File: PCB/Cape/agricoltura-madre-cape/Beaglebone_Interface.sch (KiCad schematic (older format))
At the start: 2 parts, among them P8 BeagleBone_Black_Header, P9 BeagleBone_Black_Header

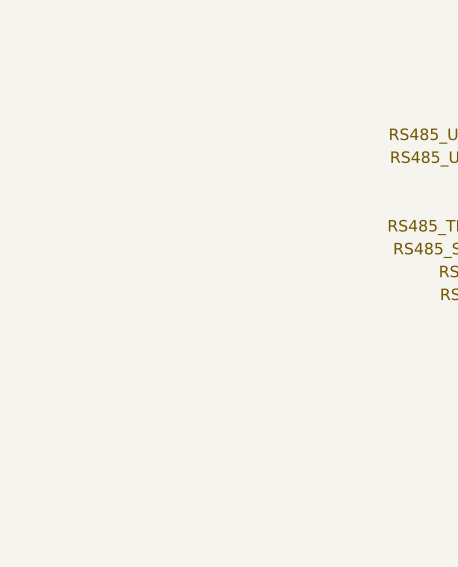
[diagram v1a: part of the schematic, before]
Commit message: SPI UART Bridge
Fleshed out schematic for SPI UART bridge chip, realized we may not need it, now going to fork project and develop two versions in this same repository.
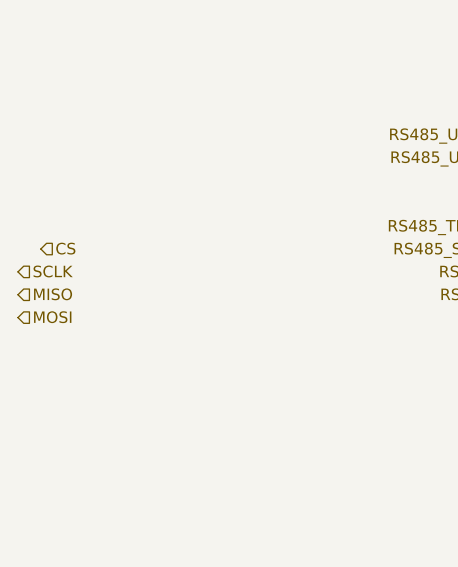
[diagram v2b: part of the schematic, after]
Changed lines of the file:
@@
 Wire Wire Line
 	3450 3550 4350 3550
+Text HLabel 1150 3650 2    50   Input ~ 0
+SCLK
+Text HLabel 1150 3750 2    50   Input ~ 0
+MISO
+Text HLabel 1150 3850 2    50   Input ~ 0
+MOSI
+Text HLabel 1250 3550 2    50   Input ~ 0
+CS
 $EndSCHEMATC

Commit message: Datasheets and BBG version
Finished initial schematic for BBG Gateway version and added datasheets for ST sub 1GHZ RF hardware.
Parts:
- added R1, R2, R3, R4, R5: RC0402FR-0733RL, AVR-KiCAD-Lib-Resistors:R0402, symbol AVR-KiCAD-Lib-Resistors:RC0402FR-0733RL
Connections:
- net CS: now also R1.1
- net MISO: now also R2.1
- net MOSI: now also R4.2
- net RS485_SL_RATE1: now also P9.20 (Pin_20); no longer P9.18 (Pin_18)
- net RS485_SL_RATE2: now also P9.27 (Pin_27); no longer P9.21 (Pin_21)
- net RS485_TERM_EN2: now also P9.29 (Pin_29); no longer P9.19 (Pin_19)
- net SCLK: now also R5.2
- net SPI0_CS0: now reaches P9.17 (Pin_17)
- net SPI0_CS0: now also R1.2
- net SPI0_SCLK: now reaches P9.22 (Pin_22)
- net SPI0_SCLK: now also R5.1
- net GNDD renamed GND
- new net: P9.19 (Pin_19), R3.2
- new net SHDN: R3.1
- new net SPI0_D0: P9.21 (Pin_21), R2.2
- new net SPI0_D1: P9.18 (Pin_18), R4.1
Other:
- moved on the sheet: P8

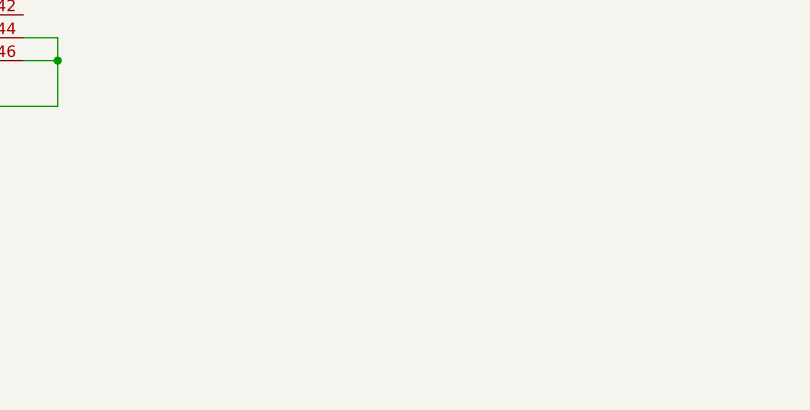
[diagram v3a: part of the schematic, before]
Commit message: Board Work
Board shape added working on cut outs
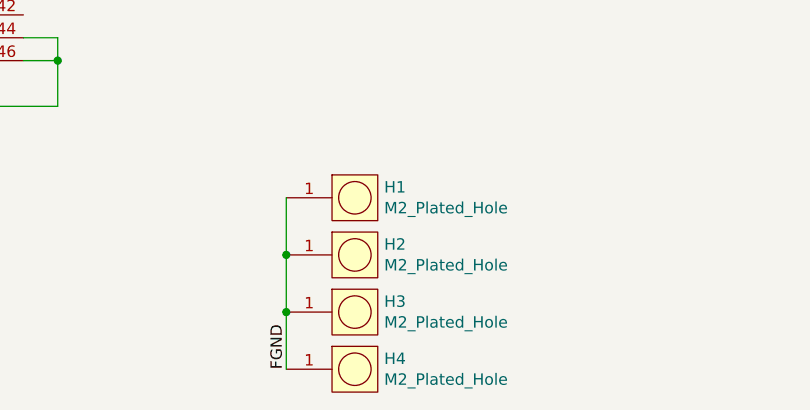
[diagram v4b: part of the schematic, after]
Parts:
- added H1, H2, H3, H4: M2_Plated_Hole, AVR-KiCAD-Lib-Holes_Fasteners:M2_HOLE, symbol AVR-KiCAD-Lib-Holes_Fasteners:M2_Plated_Hole
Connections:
- new net FGND: H1.1, H2.1, H3.1, H4.1
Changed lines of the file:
@@
 Text Label 5250 3350 0    50   ~ 0
 SPI0_D1
+$Comp
+L AVR-KiCAD-Lib-Holes_Fasteners:M2_Plated_Hole H1
+U 1 1 5F30F66E
+P 6200 5350
+F 0 "H1" H 6428 5396 50  0000 L CNN
+F 1 "M2_Plated_Hole" H 6428 5305 50  0000 L CNN
+F 2 "AVR-KiCAD-Lib-Holes_Fasteners:M2_HOLE" H 6200 5350 50  0001 C CNN
+F 3 "" H 6200 5350 50  0001 C CNN
+F 4 "*" H 6300 5600 50  0001 C CNN "Cost QTY: 1"
+F 5 "*" H 6400 5700 50  0001 C CNN "Cost QTY: 1000"
+F 6 "*" H 6500 5800 50  0001 C CNN "Cost QTY: 2500"
+F 7 "*" H 6600 5900 50  0001 C CNN "Cost QTY: 5000"
+F 8 "*" H 6700 6000 50  0001 C CNN "Cost QTY: 10000"
+F 9 "*" H 6800 6100 50  0001 C CNN "MFR"
+F 10 "*" H 6900 6200 50  0001 C CNN "MFR#"
+F 11 "*" H 7000 6300 50  0001 C CNN "Vendor"
+F 12 "*" H 7100 6400 50  0001 C CNN "Vendor #"
+F 13 "*" H 7200 6500 50  0001 C CNN "Designer"
+F 14 "*" H 7300 6600 50  0001 C CNN "Height"
+F 15 "*" H 8400 7700 50  0001 C CNN "Date Created"
+F 16 "*" H 7400 6700 50  0001 C CNN "Date Modified"
+F 17 "*" H 7500 6800 50  0001 C CNN "Lead-Free ?"
+F 18 "*" H 7600 6900 50  0001 C CNN "RoHS Levels"
+F 19 "*" H 7700 7000 50  0001 C CNN "Mounting"
+F 20 "*" H 7800 7100 50  0001 C CNN "Pin Count #"
+F 21 "*" H 7900 7200 50  0001 C CNN "Status"
+F 22 "*" H 8000 7300 50  0001 C CNN "Tolerance"
+F 23 "*" H 8100 7400 50  0001 C CNN "Type"
+F 24 "*" H 8200 7500 50  0001 C CNN "Voltage"
+F 25 "*" H 8300 7650 50  0001 C CNN "Package"
+F 26 "M2 Hole" H 8500 7850 50  0001 C CNN "_Value_"
+F 27 "*" H 8600 7950 50  0001 C CNN "Management_ID"
+F 28 "Plated M2 Screw Hole" H 8600 7950 50  0001 C CNN "Description"
+	1    6200 5350
+	1    0    0    -1
+$EndComp
+$Comp
+L AVR-KiCAD-Lib-Holes_Fasteners:M2_Plated_Hole H2
+U 1 1 5F3101E5
+P 6200 5600
+F 0 "H2" H 6428 5646 50  0000 L CNN
+F 1 "M2_Plated_Hole" H 6428 5555 50  0000 L CNN
+F 2 "AVR-KiCAD-Lib-Holes_Fasteners:M2_HOLE" H 6200 5600 50  0001 C CNN
+F 3 "" H 6200 5600 50  0001 C CNN
+F 4 "*" H 6300 5850 50  0001 C CNN "Cost QTY: 1"
+F 5 "*" H 6400 5950 50  0001 C CNN "Cost QTY: 1000"
+F 6 "*" H 6500 6050 50  0001 C CNN "Cost QTY: 2500"
+F 7 "*" H 6600 6150 50  0001 C CNN "Cost QTY: 5000"
+F 8 "*" H 6700 6250 50  0001 C CNN "Cost QTY: 10000"
+F 9 "*" H 6800 6350 50  0001 C CNN "MFR"
+F 10 "*" H 6900 6450 50  0001 C CNN "MFR#"
+F 11 "*" H 7000 6550 50  0001 C CNN "Vendor"
+F 12 "*" H 7100 6650 50  0001 C CNN "Vendor #"
+F 13 "*" H 7200 6750 50  0001 C CNN "Designer"
+F 14 "*" H 7300 6850 50  0001 C CNN "Height"
+F 15 "*" H 8400 7950 50  0001 C CNN "Date Created"
+F 16 "*" H 7400 6950 50  0001 C CNN "Date Modified"
+F 17 "*" H 7500 7050 50  0001 C CNN "Lead-Free ?"
+F 18 "*" H 7600 7150 50  0001 C CNN "RoHS Levels"
+F 19 "*" H 7700 7250 50  0001 C CNN "Mounting"
+F 20 "*" H 7800 7350 50  0001 C CNN "Pin Count #"
+F 21 "*" H 7900 7450 50  0001 C CNN "Status"
+F 22 "*" H 8000 7550 50  0001 C CNN "Tolerance"
+F 23 "*" H 8100 7650 50  0001 C CNN "Type"
+F 24 "*" H 8200 7750 50  0001 C CNN "Voltage"
+F 25 "*" H 8300 7900 50  0001 C CNN "Package"
+F 26 "M2 Hole" H 8500 8100 50  0001 C CNN "_Value_"
+F 27 "*" H 8600 8200 50  0001 C CNN "Management_ID"
+F 28 "Plated M2 Screw Hole" H 8600 8200 50  0001 C CNN "Description"
+	1    6200 5600
+	1    0    0    -1
+$EndComp
+$Comp
+L AVR-KiCAD-Lib-Holes_Fasteners:M2_Plated_Hole H3
+U 1 1 5F310E62
+P 6200 5850
+F 0 "H3" H 6428 5896 50  0000 L CNN
+F 1 "M2_Plated_Hole" H 6428 5805 50  0000 L CNN
+F 2 "AVR-KiCAD-Lib-Holes_Fasteners:M2_HOLE" H 6200 5850 50  0001 C CNN
+F 3 "" H 6200 5850 50  0001 C CNN
+F 4 "*" H 6300 6100 50  0001 C CNN "Cost QTY: 1"
+F 5 "*" H 6400 6200 50  0001 C CNN "Cost QTY: 1000"
+F 6 "*" H 6500 6300 50  0001 C CNN "Cost QTY: 2500"
+F 7 "*" H 6600 6400 50  0001 C CNN "Cost QTY: 5000"
+F 8 "*" H 6700 6500 50  0001 C CNN "Cost QTY: 10000"
+F 9 "*" H 6800 6600 50  0001 C CNN "MFR"
+F 10 "*" H 6900 6700 50  0001 C CNN "MFR#"
+F 11 "*" H 7000 6800 50  0001 C CNN "Vendor"
+F 12 "*" H 7100 6900 50  0001 C CNN "Vendor #"
+F 13 "*" H 7200 7000 50  0001 C CNN "Designer"
+F 14 "*" H 7300 7100 50  0001 C CNN "Height"
+F 15 "*" H 8400 8200 50  0001 C CNN "Date Created"
+F 16 "*" H 7400 7200 50  0001 C CNN "Date Modified"
+F 17 "*" H 7500 7300 50  0001 C CNN "Lead-Free ?"
+F 18 "*" H 7600 7400 50  0001 C CNN "RoHS Levels"
+F 19 "*" H 7700 7500 50  0001 C CNN "Mounting"
+F 20 "*" H 7800 7600 50  0001 C CNN "Pin Count #"
+F 21 "*" H 7900 7700 50  0001 C CNN "Status"
+F 22 "*" H 8000 7800 50  0001 C CNN "Tolerance"
+F 23 "*" H 8100 7900 50  0001 C CNN "Type"
+F 24 "*" H 8200 8000 50  0001 C CNN "Voltage"
+F 25 "*" H 8300 8150 50  0001 C CNN "Package"
+F 26 "M2 Hole" H 8500 8350 50  0001 C CNN "_Value_"
+F 27 "*" H 8600 8450 50  0001 C CNN "Management_ID"
+F 28 "Plated M2 Screw Hole" H 8600 8450 50  0001 C CNN "Description"
+	1    6200 5850
+	1    0    0    -1
+$EndComp
+$Comp
+L AVR-KiCAD-Lib-Holes_Fasteners:M2_Plated_Hole H4
+U 1 1 5F311B49
+P 6200 6100
+F 0 "H4" H 6428 6146 50  0000 L CNN
+F 1 "M2_Plated_Hole" H 6428 6055 50  0000 L CNN
+F 2 "AVR-KiCAD-Lib-Holes_Fasteners:M2_HOLE" H 6200 6100 50  0001 C CNN
+F 3 "" H 6200 6100 50  0001 C CNN
+F 4 "*" H 6300 6350 50  0001 C CNN "Cost QTY: 1"
+F 5 "*" H 6400 6450 50  0001 C CNN "Cost QTY: 1000"
+F 6 "*" H 6500 6550 50  0001 C CNN "Cost QTY: 2500"
+F 7 "*" H 6600 6650 50  0001 C CNN "Cost QTY: 5000"
+F 8 "*" H 6700 6750 50  0001 C CNN "Cost QTY: 10000"
+F 9 "*" H 6800 6850 50  0001 C CNN "MFR"
+F 10 "*" H 6900 6950 50  0001 C CNN "MFR#"
+F 11 "*" H 7000 7050 50  0001 C CNN "Vendor"
+F 12 "*" H 7100 7150 50  0001 C CNN "Vendor #"
+F 13 "*" H 7200 7250 50  0001 C CNN "Designer"
+F 14 "*" H 7300 7350 50  0001 C CNN "Height"
+F 15 "*" H 8400 8450 50  0001 C CNN "Date Created"
+F 16 "*" H 7400 7450 50  0001 C CNN "Date Modified"
+F 17 "*" H 7500 7550 50  0001 C CNN "Lead-Free ?"
+F 18 "*" H 7600 7650 50  0001 C CNN "RoHS Levels"
+F 19 "*" H 7700 7750 50  0001 C CNN "Mounting"
+F 20 "*" H 7800 7850 50  0001 C CNN "Pin Count #"
+F 21 "*" H 7900 7950 50  0001 C CNN "Status"
+F 22 "*" H 8000 8050 50  0001 C CNN "Tolerance"
+F 23 "*" H 8100 8150 50  0001 C CNN "Type"
+F 24 "*" H 8200 8250 50  0001 C CNN "Voltage"
+F 25 "*" H 8300 8400 50  0001 C CNN "Package"
+F 26 "M2 Hole" H 8500 8600 50  0001 C CNN "_Value_"
+F 27 "*" H 8600 8700 50  0001 C CNN "Management_ID"
+F 28 "Plated M2 Screw Hole" H 8600 8700 50  0001 C CNN "Description"
+	1    6200 6100
+	1    0    0    -1
+$EndComp
+Wire Wire Line
+	6000 5350 6000 5600
+Connection ~ 6000 5600
+Wire Wire Line
+	6000 5600 6000 5850
+Connection ~ 6000 5850
+Wire Wire Line
+	6000 5850 6000 6100
+Text Label 6000 6100 1    50   ~ 0
+FGND
 $EndSCHEMATC
